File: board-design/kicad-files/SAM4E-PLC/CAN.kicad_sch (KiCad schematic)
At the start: 65 parts, among them U10 MAX31865xAP, U6 SN65HVD230DR, U7 SN65HVD230DR, U8 MAX31865xAP, U9 MAX3485

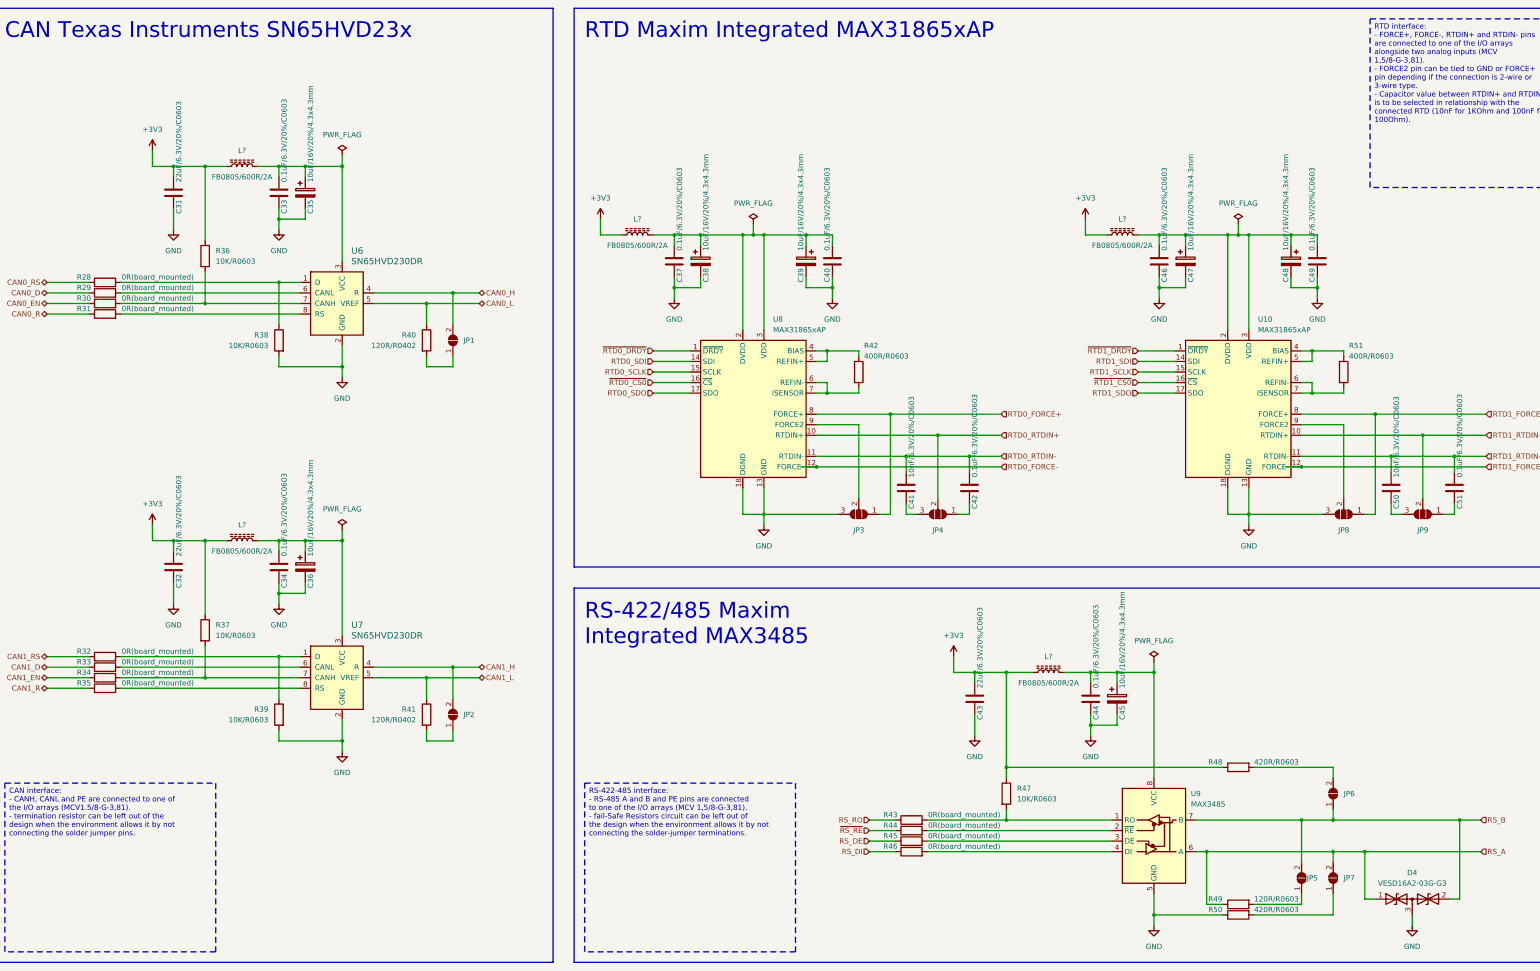
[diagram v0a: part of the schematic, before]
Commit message: [UPDATE]
Refactored schematic for LTE, Power and other schematic sub-sheets.

Signed-off-by: Nicolae-Andrei Vasile <vasilenicolaeandrei@gmail.com>
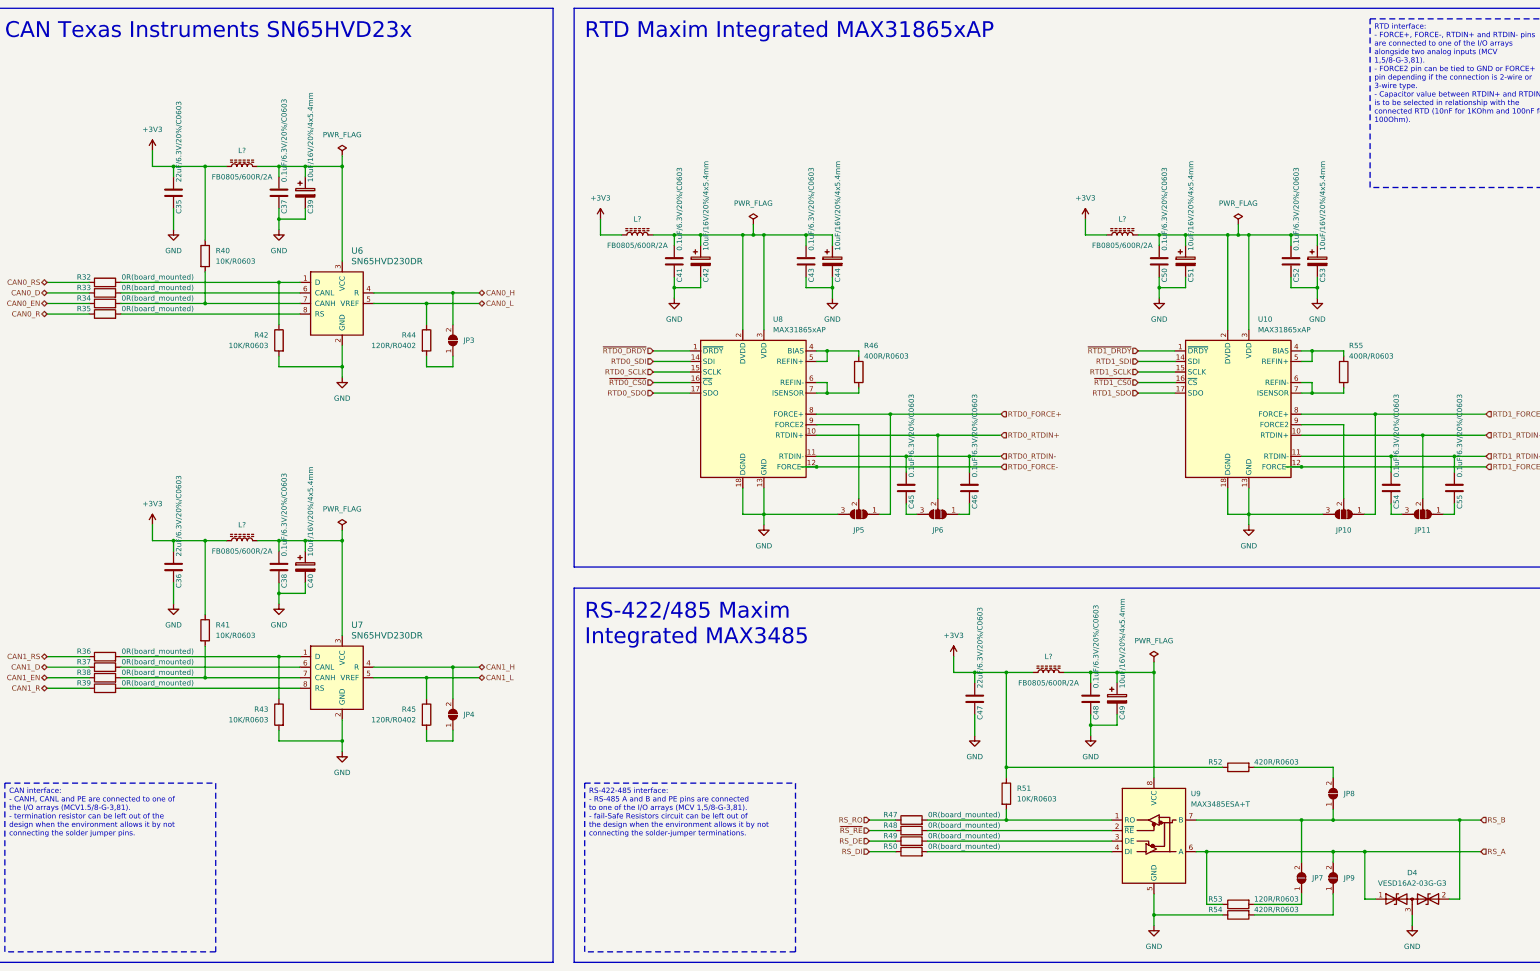
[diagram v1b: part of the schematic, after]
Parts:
- removed C31: 22uF/6.3V/20%/C0603, symbol Device:C
- removed C36, C38, C39, C45, C47, C48: 10uF/16V/20%/4.3x4.3mm, symbol Device:C_Polarized
- removed C37, C40, C42, C44, C49, C51: 0.1uF/6.3V/20%/C0603, symbol Device:C
- removed JP3, JP4, JP8: SolderJumper_3_Open, symbol Jumper:SolderJumper_3_Open
- removed JP5: SolderJumper_2_Open, symbol Jumper:SolderJumper_2_Open
- removed L? (x5): FB0805/600R/2A, symbol Device:L_Ferrite
- removed R28, R29, R30, R31, R43, R44, R45, R46: 0R(board_mounted), symbol Device:R
- added C35, C47: 22uF/6.3V/20%/C0603, Capacitor_SMD:C_0603_1608Metric, symbol Device:C
- added C40, C42, C44, C49, C51, C53: 10uF/16V/20%/4x5.4mm, Capacitor_SMD:CP_Elec_4x5.4, symbol Device:C_Polarized
- added C45, C48, C52, C54, C55: 0.1uF/6.3V/20%/C0603, Capacitor_SMD:C_0603_1608Metric, symbol Device:C
- added JP10, JP5, JP6: SolderJumper_3_Open, Jumper:SolderJumper-3_P1.3mm_Open_Pad1.0x1.5mm, symbol Jumper:SolderJumper_3_Open
- added JP9: SolderJumper_2_Open, Jumper:SolderJumper-2_P1.3mm_Open_Pad1.0x1.5mm, symbol Jumper:SolderJumper_2_Open
- added L? (x5): FB0805/600R/2A, Inductor_SMD:L_0805_2012Metric, symbol Device:L_Ferrite
- added R32, R37, R38, R39, R48, R49, R50: 0R(board_mounted), Resistor_SMD:R_0402_1005Metric, symbol Device:R
- added R51: 10K/R0603, Resistor_SMD:R_0603_1608Metric, symbol Device:R
- C36: renamed from C32; footprint (none) -> Capacitor_SMD:C_0603_1608Metric
- C37: renamed from C33; footprint (none) -> Capacitor_SMD:C_0603_1608Metric
- C38: renamed from C34; footprint (none) -> Capacitor_SMD:C_0603_1608Metric
- C39: renamed from C35; value 10uF/16V/20%/4.3x4.3mm -> 10uF/16V/20%/4x5.4mm; footprint (none) -> Capacitor_SMD:CP_Elec_4x5.4
- C41, C50: value 10nF/6.3V/20%/C0603 -> 0.1uF/6.3V/20%/C0603; footprint (none) -> Capacitor_SMD:C_0603_1608Metric
- C43: value 22uF/6.3V/20%/C0603 -> 0.1uF/6.3V/20%/C0603; footprint (none) -> Capacitor_SMD:C_0603_1608Metric
- C46: footprint (none) -> Capacitor_SMD:C_0603_1608Metric
- JP11: renamed from JP9; footprint (none) -> Jumper:SolderJumper-3_P1.3mm_Open_Pad1.0x1.5mm
- JP7: footprint (none) -> Jumper:SolderJumper-2_P1.3mm_Open_Pad1.0x1.5mm
- JP8: renamed from JP6; footprint (none) -> Jumper:SolderJumper-2_P1.3mm_Open_Pad1.0x1.5mm
- R33, R34, R35: footprint (none) -> Resistor_SMD:R_0402_1005Metric
- R36: renamed from R32; footprint (none) -> Resistor_SMD:R_0402_1005Metric
- R40: renamed from R36; footprint (none) -> Resistor_SMD:R_0603_1608Metric
- R41: renamed from R37; footprint (none) -> Resistor_SMD:R_0603_1608Metric
- R42: renamed from R38; footprint (none) -> Resistor_SMD:R_0603_1608Metric
- R43: renamed from R39; footprint (none) -> Resistor_SMD:R_0603_1608Metric
- R46: renamed from R42; footprint (none) -> Resistor_SMD:R_0603_1608Metric
- R47: value 10K/R0603 -> 0R(board_mounted); footprint (none) -> Resistor_SMD:R_0402_1005Metric
- R52: renamed from R48; footprint (none) -> Resistor_SMD:R_0603_1608Metric
- R53: renamed from R49; footprint (none) -> Resistor_SMD:R_0603_1608Metric
- R54: renamed from R50; footprint (none) -> Resistor_SMD:R_0603_1608Metric
- R55: renamed from R51; footprint (none) -> Resistor_SMD:R_0603_1608Metric
- U9: value MAX3485 -> MAX3485ESA+T; footprint (none) -> Package_SO:SO-8_3.9x4.9mm_P1.27mm
- renumbered JP1 to JP3, JP2 to JP4, R40 to R44, R41 to R45
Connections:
- net +3V3: now also C35.1, C47.1, L?.1, L?.1, L?.1, L?.1, L?.1, R51.1; no longer C43.1, R47.1
- net CAN0_D: now also R33.1
- net CAN0_EN: now also R34.1
- net CAN0_R: now also R35.1
- net CAN0_RS: now also R32.1
- net CAN1_D: now also R37.1; no longer R33.1
- net CAN1_EN: now also R38.1; no longer R34.1
- net CAN1_R: now also R39.1; no longer R35.1
- net GND: now also C41.2, C50.2, C35.2, C40.2, C42.2, C44.2, C47.2, C48.2, C49.2, C51.2, C52.2, C53.2, JP10.3 (B), JP5.3 (B); no longer C46.2
- net RS_A: now also JP9.2 (B); no longer JP7.2 (B)
- net RS_B: now also JP7.2 (B)
- net RS_DE: now also R49.1
- net RS_DI: now also R50.1
- net RS_RO: now also R47.1
- net RTD0_FORCE+: now also JP5.1 (A)
- net RTD0_RTDIN+: now also JP6.2 (C)
- net RTD0_RTDIN-: now also C46.1, C45.1; no longer C41.1
- net RTD1_FORCE+: now also JP10.1 (A)
- net RTD1_RTDIN-: now also C54.1, C55.1; no longer C50.1
- net ~{RS_RE}: now also R48.1
- net at C37.1, C39.1, U6.3 (VCC): now also L?.2
- net at U10.2 (DVDD), U10.3 (VDD): now also C50.1, C51.1, C52.1, C53.1, L?.2; no longer C46.1
- net at U10.9 (FORCE2): now also JP10.2 (C)
- net at R47.2, U9.1 (RO): now also R51.2
- net at U9.2 (~{RE}): now also R48.2
- net at U9.3 (DE): now also R49.2
- net at U9.4 (DI): now also R50.2
- net at U9.8 (VCC): now also C48.1, C49.1, L?.2
- net at R54.2: now also JP9.1 (A); no longer JP7.1 (A)
- net at U8.2 (DVDD), U8.3 (VDD): now also C41.1, C43.1, C42.1, C44.1, L?.2
- net at R42.1, U6.1 (D): now also R32.2
- net at JP11.3 (B): now also C54.2; no longer C50.2
- net at U7.6 (CANL): now also R37.2; no longer R33.2
- net at U6.8 (RS): now also R35.2
- net at U8.9 (FORCE2): now also JP5.2 (C)
- net at R41.2, U7.7 (CANH): now also R38.2; no longer R34.2
- net at C38.1, U7.3 (VCC): now also C40.1, L?.2
- net at U6.6 (CANL): now also R33.2
- net at R40.2, U6.7 (CANH): now also R34.2
- net at U7.8 (RS): now also R39.2; no longer R35.2
- net at R53.2: now also JP7.1 (A)
- net at JP11.1 (A): now also C55.2
- new net: C46.2, JP6.1 (A)
- new net: C45.2, JP6.3 (B)
